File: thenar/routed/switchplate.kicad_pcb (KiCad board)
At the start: 2 copper layers, 130.7 x 105.1 mm, 5 parts

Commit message: feat(scaffold): auto GND pour + title-block via pcbnew Python
Two pcbnew Python passes wired into the scaffold derivation:

1. Title block populated (Title=Thenar, Company=lytedev, Rev=1.0,
   comments with repo link + description). Previously KiCad showed
   placeholder 'Unknown' and 'keyboard'.

2. F.Cu + B.Cu GND filled zones added covering the board outline. This
   means GND does not need to be hand-routed: every GND-net pad ties
   into the plane automatically. Zones are saved unfilled; gerber export
   passes --check-zones to fill them at fab-output time.

Implementation gotchas that cost a chunk of debugging:

- pcbnew Python segfaults on SaveBoard if the input is KiCad 5.1 format
  (which is what ergogen emits). Solved by running 'kicad-cli pcb
  upgrade' in the scaffold step before invoking pcbnew.
- pcbnew.ZONE.SetOutline takes ownership of a SHAPE_POLY_SET, but Python
  reference counting also wants to free it - double-free crash at save.
  Switched to AppendCorner which copies coordinates instead.
- pcbnew needs a writable HOME for wxConfig. Build derivation sets
  HOME=mktemp -d.

routing.md updated: GND is no longer in the route-by-hand list.
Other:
- net class Default removed

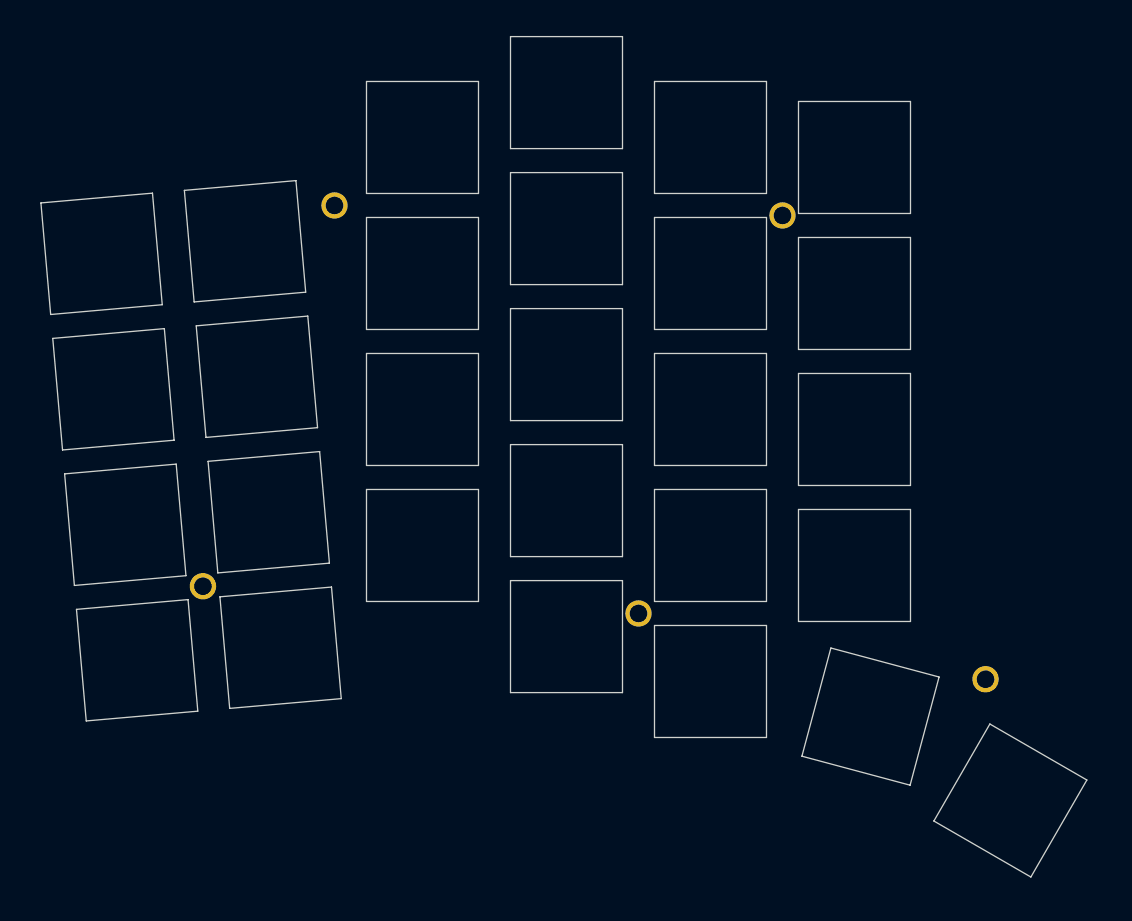
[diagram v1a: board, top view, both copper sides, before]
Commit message: feat(ergogen): close the outline polygon at the outer-num corner
The outline definition added matrix_outer_num top-LEFT followed by top-RIGHT
between outer_top and pinky_num. Because pinky_num top-left is slightly LEFT
of outer_num top-right (pinky column is +1kx, but the polygon shift offsets
collapse the gap to under 2mm), the polygon backtracks at that corner. With
fillet=2 ergogen produces an outline with a non-closing gap there, breaking
DSN export and tripping KiCad's invalid_outline DRC check.

Fix: drop the redundant outer_num top-right point. The polygon now goes
outer_top top-left -> outer_num top-left -> pinky_num top-left, the same
left-edge-then-diagonal shape that worked for the upstream corax. DRC
reports zero invalid_outline violations now.

Also adds a freerouting orchestration script (thenar/scripts/autoroute.py)
that handles the DSN->freerouting->SES roundtrip, but does not wire it
into the flake: the reversible PCB has intentionally-shorted hybrid nets
(NN_GND_SCL etc.) that KiCad's DSN exporter refuses, so the script
currently bails. Docstring documents what a flattening pre-pass would
need to do. routing.md links to this status.

Bumps gitignore: keyboard-drc.rpt and *.kicad_prl (auto-created by KiCad).
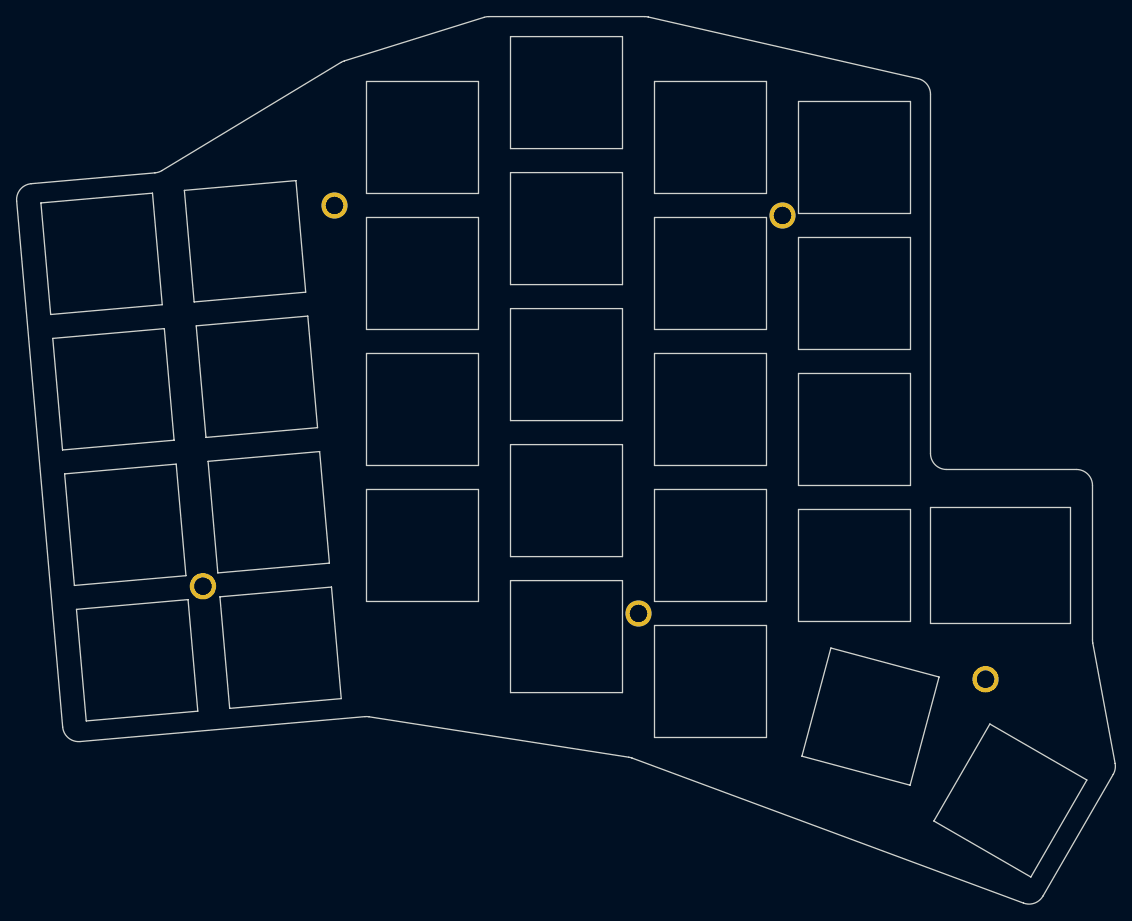
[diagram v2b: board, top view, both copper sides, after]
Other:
- board size 130.7 x 105.1 mm -> 137.3 x 110.9 mm
